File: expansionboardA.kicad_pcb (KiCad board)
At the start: 2 copper layers, 111 x 109.4 mm, 40 parts, among them J1 USB-SERIAL, J3 HDMI_A, P1 USB_C_Plug, U1 MAX3420EECJ, U2 GPIO_U2, U3 AMS1117-3.3, U4 GPIO_U4, U5 MCP3008T-I/SL, U6 TLV320AIC23BIPW, Y1 Crystal

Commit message: Small layout edits
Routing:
- net LED4: track 44.6 -> 42.3 mm
- net LED3: track 47.5 -> 46.6 mm
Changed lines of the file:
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@@
     (property "ki_keywords" "cap capacitor")
     (attr smd)
-    (fp_text reference "C2" (at 0 -1.43 45) (layer "F.SilkS")
+    (fp_text reference "C2" (at -0.833029 -1.885661 45) (layer "F.SilkS")
         (effects (font (size 1 1) (thickness 0.15)))
     )
@@
     (property "ki_keywords" "cap capacitor")
     (attr smd)
-    (fp_text reference "C7" (at 3.1308 0.1256 -270) (layer "F.SilkS")
+    (fp_text reference "C7" (at 2.9972 0.0254 -270) (layer "F.SilkS")
         (effects (font (size 1 1) (thickness 0.15)))
     )
@@
     (property "ki_keywords" "cap capacitor")
     (attr smd)
-    (fp_text reference "C4" (at -3.355917 -0.179605 45) (layer "F.SilkS")
+    (fp_text reference "C4" (at -0.087104 -1.975656 45) (layer "F.SilkS")
         (effects (font (size 1 1) (thickness 0.15)))
     )
@@
     (property "ki_keywords" "quartz ceramic resonator oscillator")
     (attr through_hole)
-    (fp_text reference "Y1" (at -1.75 -3 -225) (layer "B.SilkS")
+    (fp_text reference "Y1" (at -1.752563 -7.848744 -225) (layer "B.SilkS")
         (effects (font (size 1 1) (thickness 0.15)) (justify mirror))
     )
@@
   (via (at 42.926 69.088) (size 0.8) (drill 0.4) (layers "F.Cu" "B.Cu") (net 108))
   (segment (start 33.2232 87.376) (end 31.6992 87.376) (width 0.25) (layer "B.Cu") (net 108))
-  (segment (start 46.99 66.6496) (end 46.99 44.41) (width 0.25) (layer "B.Cu") (net 108))
   (segment (start 45.68 43.18) (end 48.22 43.18) (width 0.25) (layer "B.Cu") (net 108))
   (segment (start 30.9118 84.4296) (end 31.7754 83.566) (width 0.25) (layer "B.Cu") (net 108))
   (segment (start 103.124 44.704) (end 95.25 44.704) (width 0.25) (layer "B.Cu") (net 108))
+  (segment (start 44.704 67.31) (end 46.3296 67.31) (width 0.25) (layer "B.Cu") (net 108))
   (segment (start 103.124 44.704) (end 104.648 43.18) (width 0.25) (layer "B.Cu") (net 108))
   (segment (start 88.646 38.1) (end 79.248 38.1) (width 0.25) (layer "B.Cu") (net 108))
-  (segment (start 42.926 69.088) (end 44.704 67.31) (width 0.25) (layer "B.Cu") (net 108))
   (segment (start 31.7754 83.566) (end 32.512 83.566) (width 0.25) (layer "B.Cu") (net 108))
-  (segment (start 44.704 67.31) (end 46.3296 67.31) (width 0.25) (layer "B.Cu") (net 108))
+  (segment (start 46.3296 67.31) (end 46.9392 66.7004) (width 0.25) (layer "B.Cu") (net 108))
+  (segment (start 42.926 69.088) (end 44.704 67.31) (width 0.25) (layer "B.Cu") (net 108))
   (segment (start 112.268 74.93) (end 105.791 74.93) (width 0.25) (layer "B.Cu") (net 108))
   (segment (start 30.9118 86.5886) (end 30.9118 84.4296) (width 0.25) (layer "B.Cu") (net 108))
   (segment (start 103.124 72.263) (end 103.124 44.704) (width 0.25) (layer "B.Cu") (net 108))
   (segment (start 70.612 29.464) (end 65.106 29.464) (width 0.25) (layer "B.Cu") (net 108))
+  (segment (start 46.9392 66.7004) (end 46.9392 44.4608) (width 0.25) (layer "B.Cu") (net 108))
   (segment (start 33.782 119.6594) (end 33.782 87.9348) (width 0.25) (layer "B.Cu") (net 108))
   (segment (start 106.68 43.18) (end 109.22 43.18) (width 0.25) (layer "B.Cu") (net 108))
-  (segment (start 46.99 44.41) (end 48.22 43.18) (width 0.25) (layer "B.Cu") (net 108))
   (segment (start 82.7786 124.968) (end 39.0906 124.968) (width 0.25) (layer "B.Cu") (net 108))
   (segment (start 39.0906 124.968) (end 33.782 119.6594) (width 0.25) (layer "B.Cu") (net 108))
+  (segment (start 46.9392 44.4608) (end 48.22 43.18) (width 0.25) (layer "B.Cu") (net 108))
   (segment (start 95.25 44.704) (end 88.646 38.1) (width 0.25) (layer "B.Cu") (net 108))
   (segment (start 31.6992 87.376) (end 30.9118 86.5886) (width 0.25) (layer "B.Cu") (net 108))
   (segment (start 104.648 43.18) (end 106.68 43.18) (width 0.25) (layer "B.Cu") (net 108))
-  (segment (start 46.3296 67.31) (end 46.99 66.6496) (width 0.25) (layer "B.Cu") (net 108))
   (segment (start 105.791 74.93) (end 103.124 72.263) (width 0.25) (layer "B.Cu") (net 108))
   (segment (start 82.8294 124.9172) (end 82.7786 124.968) (width 0.25) (layer "B.Cu") (net 108))
@@
   (segment (start 57.125 74.825) (end 49.385 74.825) (width 0.25) (layer "F.Cu") (net 142))
   (segment (start 49.385 74.825) (end 48.22 73.66) (width 0.25) (layer "F.Cu") (net 142))
+  (segment (start 82.036584 32.5738) (end 84.827792 32.5738) (width 0.25) (layer "F.Cu") (net 154))
+  (segment (start 85.277792 32.1238) (end 92.3098 32.1238) (width 0.25) (layer "F.Cu") (net 154))
+  (segment (start 92.3098 32.1238) (end 93.5736 30.86) (width 0.25) (layer "F.Cu") (net 154))
+  (segment (start 84.827792 32.5738) (end 85.277792 32.1238) (width 0.25) (layer "F.Cu") (net 154))
+  (segment (start 80.7174 33.0238) (end 81.586584 33.0238) (width 0.25) (layer "F.Cu") (net 154))
   (segment (start 48.22 66.04) (end 48.22 65.5212) (width 0.25) (layer "F.Cu") (net 154))
-  (segment (start 48.22 65.5212) (end 67.737368 46.003832) (width 0.25) (layer "F.Cu") (net 154))
-  (segment (start 67.737368 46.003832) (end 71.62636 46.003832) (width 0.25) (layer "F.Cu") (net 154))
-  (segment (start 92.3986 32.035) (end 93.5736 30.86) (width 0.25) (layer "F.Cu") (net 154))
-  (segment (start 71.62636 46.003832) (end 85.595192 32.035) (width 0.25) (layer "F.Cu") (net 154))
-  (segment (start 85.595192 32.035) (end 92.3986 32.035) (width 0.25) (layer "F.Cu") (net 154))
-  (segment (start 49.604804 63.5) (end 67.550972 45.553832) (width 0.25) (layer "F.Cu") (net 155))
-  (segment (start 89.4577 31.585) (end 90.1827 30.86) (width 0.25) (layer "F.Cu") (net 155))
-  (segment (start 71.439964 45.553832) (end 85.408796 31.585) (width 0.25) (layer "F.Cu") (net 155))
-  (segment (start 85.408796 31.585) (end 89.4577 31.585) (width 0.25) (layer "F.Cu") (net 155))
+  (segment (start 48.22 65.5212) (end 80.7174 33.0238) (width 0.25) (layer "F.Cu") (net 154))
+  (segment (start 81.586584 33.0238) (end 82.036584 32.5738) (width 0.25) (layer "F.Cu") (net 154))
+  (segment (start 85.091396 31.6738) (end 87.8332 31.6738) (width 0.25) (layer "F.Cu") (net 155))
+  (segment (start 88.647 30.86) (end 90.1827 30.86) (width 0.25) (layer "F.Cu") (net 155))
+  (segment (start 80.531004 32.5738) (end 81.400188 32.5738) (width 0.25) (layer "F.Cu") (net 155))
   (segment (start 48.22 63.5) (end 49.604804 63.5) (width 0.25) (layer "F.Cu") (net 155))
-  (segment (start 67.550972 45.553832) (end 71.439964 45.553832) (width 0.25) (layer "F.Cu") (net 155))
-  (segment (start 85.4974 30.86) (end 86.7918 30.86) (width 0.25) (layer "F.Cu") (net 156))
-  (segment (start 51.508408 60.96) (end 67.364576 45.103832) (width 0.25) (layer "F.Cu") (net 156))
-  (segment (start 71.253568 45.103832) (end 85.4974 30.86) (width 0.25) (layer "F.Cu") (net 156))
-  (segment (start 67.364576 45.103832) (end 71.253568 45.103832) (width 0.25) (layer "F.Cu") (net 156))
+  (segment (start 49.604804 63.5) (end 80.531004 32.5738) (width 0.25) (layer "F.Cu") (net 155))
+  (segment (start 84.641396 32.1238) (end 85.091396 31.6738) (width 0.25) (layer "F.Cu") (net 155))
+  (segment (start 81.400188 32.5738) (end 81.850188 32.1238) (width 0.25) (layer "F.Cu") (net 155))
+  (segment (start 81.850188 32.1238) (end 84.641396 32.1238) (width 0.25) (layer "F.Cu") (net 155))
+  (segment (start 87.8332 31.6738) (end 88.647 30.86) (width 0.25) (layer "F.Cu") (net 155))
+  (segment (start 51.508408 60.96) (end 80.344608 32.1238) (width 0.25) (layer "F.Cu") (net 156))
+  (segment (start 85.2688 30.86) (end 86.7918 30.86) (width 0.25) (layer "F.Cu") (net 156))
   (segment (start 48.22 60.96) (end 51.508408 60.96) (width 0.25) (layer "F.Cu") (net 156))
-  (segment (start 71.067172 44.653832) (end 83.4009 32.320104) (width 0.25) (layer "F.Cu") (net 157))
-  (segment (start 67.17818 44.653832) (end 71.067172 44.653832) (width 0.25) (layer "F.Cu") (net 157))
-  (segment (start 83.4009 32.320104) (end 83.4009 30.86) (width 0.25) (layer "F.Cu") (net 157))
+  (segment (start 84.455 31.6738) (end 85.2688 30.86) (width 0.25) (layer "F.Cu") (net 156))
+  (segment (start 80.344608 32.1238) (end 81.213792 32.1238) (width 0.25) (layer "F.Cu") (net 156))
+  (segment (start 81.663792 31.6738) (end 84.455 31.6738) (width 0.25) (layer "F.Cu") (net 156))
+  (segment (start 81.213792 32.1238) (end 81.663792 31.6738) (width 0.25) (layer "F.Cu") (net 156))
   (segment (start 48.22 58.42) (end 53.412012 58.42) (width 0.25) (layer "F.Cu") (net 157))
-  (segment (start 53.412012 58.42) (end 67.17818 44.653832) (width 0.25) (layer "F.Cu") (net 157))
-  (segment (start 70.880776 44.203832) (end 80.01 35.074608) (width 0.25) (layer "F.Cu") (net 158))
-  (segment (start 80.01 35.074608) (end 80.01 30.86) (width 0.25) (layer "F.Cu") (net 158))
+  (segment (start 80.158212 31.6738) (end 81.027396 31.6738) (width 0.25) (layer "F.Cu") (net 157))
+  (segment (start 81.027396 31.6738) (end 81.841196 30.86) (width 0.25) (layer "F.Cu") (net 157))
+  (segment (start 81.841196 30.86) (end 83.4009 30.86) (width 0.25) (layer "F.Cu") (net 157))
+  (segment (start 53.412012 58.42) (end 80.158212 31.6738) (width 0.25) (layer "F.Cu") (net 157))
+  (segment (start 80.01 31.185616) (end 80.01 30.86) (width 0.25) (layer "F.Cu") (net 158))
+  (segment (start 55.315616 55.88) (end 80.01 31.185616) (width 0.25) (layer "F.Cu") (net 158))
   (segment (start 48.22 55.88) (end 55.315616 55.88) (width 0.25) (layer "F.Cu") (net 158))
-  (segment (start 66.991784 44.203832) (end 70.880776 44.203832) (width 0.25) (layer "F.Cu") (net 158))
-  (segment (start 55.315616 55.88) (end 66.991784 44.203832) (width 0.25) (layer "F.Cu") (net 158))
   (segment (start 89.696427 94.453573) (end 89.488571 94.453573) (width 0.25) (layer "F.Cu") (net 159))
   (segment (start 89.488571 94.453573) (end 84.9122 89.877202) (width 0.25) (layer "F.Cu") (net 159))

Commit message: Board updated
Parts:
- moved ADC1 10.0 mm to (35.1, 93.6)
- moved C2 1.83 mm to (82.9, 102.7), turned to 0 degrees
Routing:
- net USBSCLK: track 49.7 -> 68.5 mm
- net HPOUTRIGHT: track 74.0 -> 91.4 mm
- net USBMISO: track 53.8 -> 68.5 mm
- net LINEOUTRIGHT: track 78.7 -> 91.6 mm
- net USBGPX: track 57.4 -> 68.5 mm
- net ADCH1: track 24.0 -> 34.9 mm
- net USBMOSI: track 58.6 -> 68.5 mm
- net ADCH3: track 19.7 -> 29.2 mm
- net ADCH4: track 15.5 -> 24.8 mm
- net ADCH5: track 16.3 -> 25.4 mm
- net ADCH2: track 22.1 -> 31.2 mm
- net ADCH6: track 9.13 -> 18.2 mm
- net ADCH0: track 28.9 -> 37.9 mm
- net ADCH7: track 12.4 -> 21.1 mm
- net LINEOUTLEFT: track 83.3 -> 91.7 mm
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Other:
- board text added: "DVI OUT"
- board text added: "INT"
- board text added: "REG 3V"
- board text removed: "Video Out"

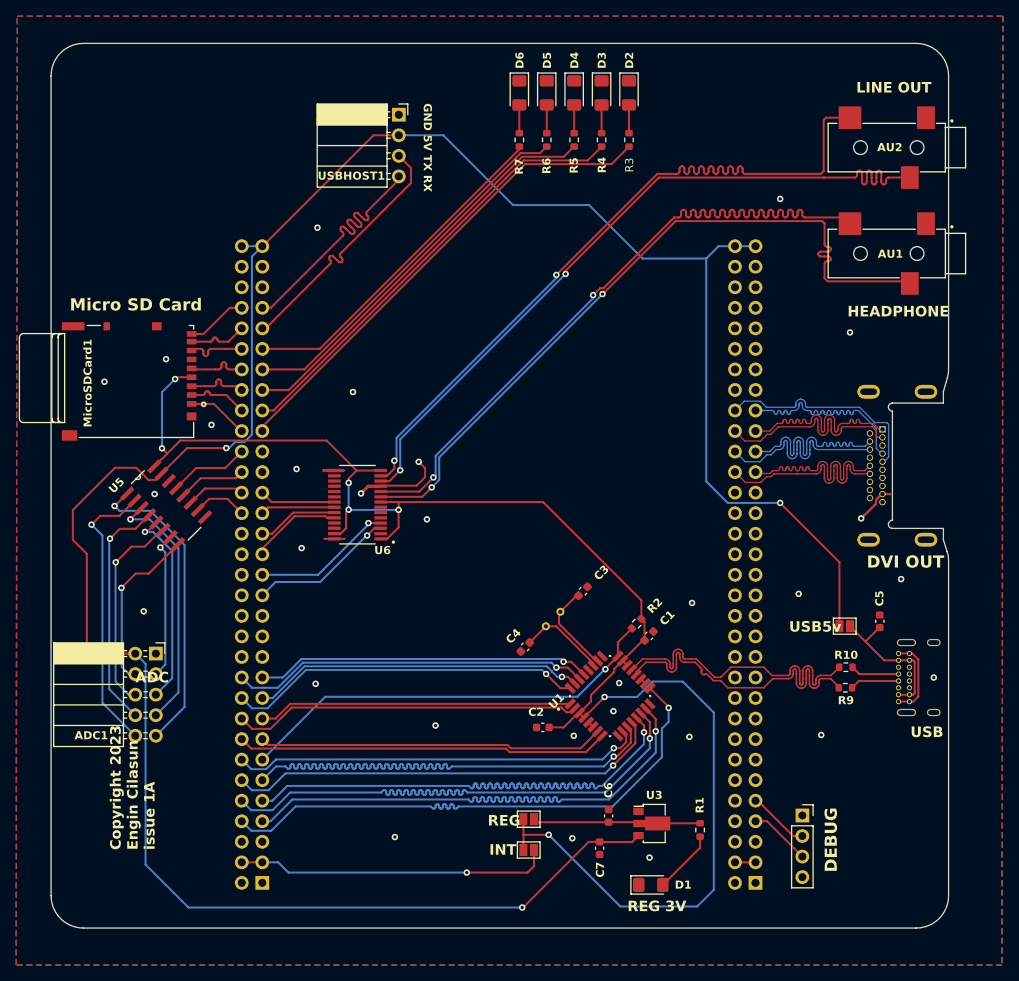
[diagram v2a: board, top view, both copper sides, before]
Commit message: Updated schematic with correct parts Built gerber files
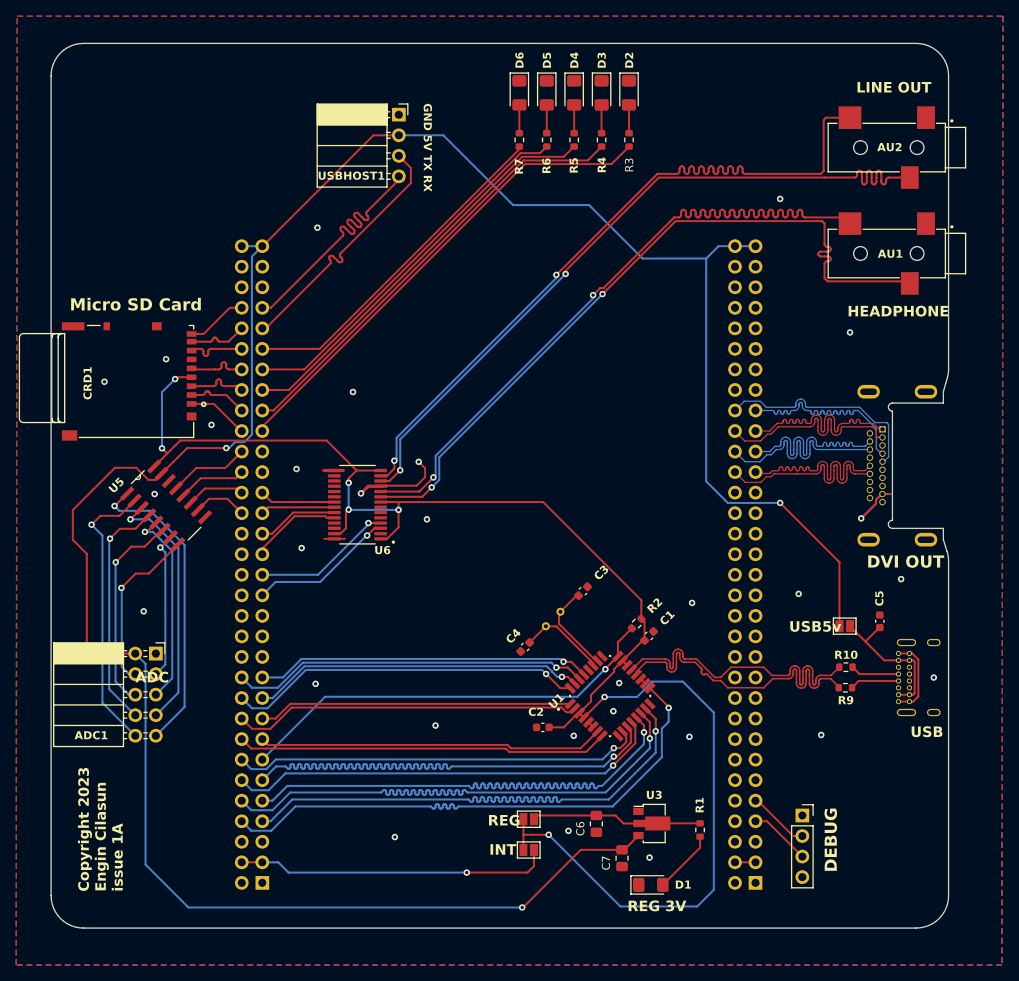
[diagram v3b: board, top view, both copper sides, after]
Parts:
- C6, C7: footprint Capacitor_SMD:C_0603_1608Metric -> Capacitor_SMD:C_0805_2012Metric_Pad1.18x1.45mm_HandSolder
- J1: value USB-SERIAL -> DEBUG
- moved C7 3.04 mm to (92.7, 118.9)
- moved C6 1.82 mm to (89.5, 114.6), turned to -90 degrees
- renumbered MicroSDCard1 to CRD1
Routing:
- net 5V: track 301.7 -> 300.6 mm

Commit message: Updated board with USB A host connector
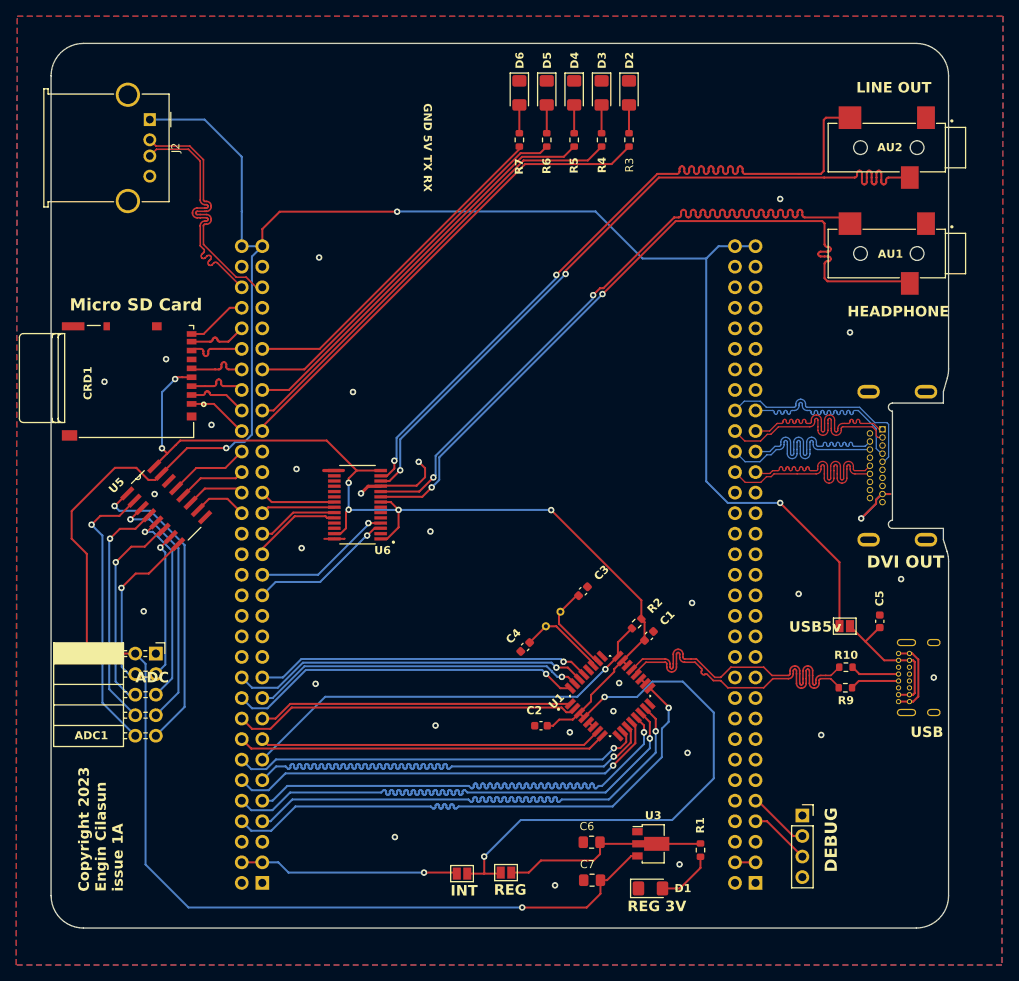
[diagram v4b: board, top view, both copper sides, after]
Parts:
- removed USBHOST1: Conn_01x4_Socket, Connector_PinSocket_2.54mm:PinSocket_1x04_P2.54mm_Horizontal
- added J2: USB_A_Stacked, Connector_USB:USB_A_Molex_67643_Horizontal, F.Cu at (34.3, 27.5)
- moved JP6 8.75 mm to (72.9, 120.8), turned to 180 degrees
- moved JP5 7.18 mm to (78.4, 120.7)
- moved C7 4.59 mm to (89.0, 121.6), turned to 180 degrees
- moved U3 2.52 mm to (96.6, 117.1)
- moved R1 2.49 mm to (102.4, 117.9)
- moved C6 2.34 mm to (89.0, 116.9), turned to 180 degrees
- moved D1 0.43 mm to (96.2, 122.6)
- moved C2 0.31 mm to (82.7, 102.5)
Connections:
- U2 pad 55: USBTX -> unconnected-(U2-Pin_55-Pad55)
- U2 pad 57: USBRX -> unconnected-(U2-Pin_57-Pad57)
- U2 pad 59: unconnected-(U2-Pin_59-Pad59) -> USBD1_N
- U2 pad 60: unconnected-(U2-Pin_60-Pad60) -> USBD1_P
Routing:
- net USBTX: track 32.0 -> 0.00 mm
- net USBD1_N: track 0.00 -> 31.9 mm
- net USBRX: track 31.9 -> 0.00 mm
- net USBD1_P: track 0.00 -> 31.8 mm
- net 5V: track 300.6 -> 318.3 mm, vias 3 -> 4
- net 3V3: track 39.0 -> 27.2 mm
- net /input3v3: track 198.9 -> 191.1 mm, vias 7 -> 8
- net REG3V3: track 21.2 -> 25.9 mm
- net Net-(D1-A): track 7.88 -> 7.12 mm

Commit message: Updated board
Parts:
- C1, C2, C3, C4, C5: footprint Capacitor_SMD:C_0603_1608Metric -> Capacitor_SMD:C_0603_1608Metric_Pad1.08x0.95mm_HandSolder
- R1, R10, R2, R3, R4, R5, R6, R7, R9: footprint Resistor_SMD:R_0603_1608Metric -> Resistor_SMD:R_0603_1608Metric_Pad0.98x0.95mm_HandSolder
- U3: footprint Package_TO_SOT_SMD:SOT-89-3 -> Package_TO_SOT_SMD:SOT-89-3_Handsoldering
- moved D3 28.1 mm to (62.1, 23.9)
- moved D4 28.1 mm to (58.7, 23.9)
- moved D5 28.1 mm to (55.3, 23.9)
- moved D6 28.1 mm to (51.9, 23.9)
- moved R7 28.1 mm to (51.9, 29.8)
- moved R3 28.1 mm to (65.5, 29.8)
- moved R4 28.1 mm to (62.1, 29.8)
- moved R5 28.1 mm to (58.7, 29.8)
- moved R6 28.1 mm to (55.3, 29.8)
- moved D2 28.1 mm to (65.5, 23.9)
- moved C3 0.21 mm to (87.9, 85.6)
- moved C2 0.19 mm to (82.5, 102.5)
- moved C4 0.13 mm to (80.6, 92.8)
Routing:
- net LED3: track 46.6 -> 31.5 mm
- net LED2: track 51.0 -> 36.8 mm
- net LED1: track 55.5 -> 41.9 mm
- net LED4: track 42.3 -> 29.6 mm
- net LED0: track 60.2 -> 48.0 mm
- net 5V: track 318.3 -> 318.9 mm
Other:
- board text added: "5V D- D+ GND"
- board text added: "Copyright 2023 Engin Cilasun issue 1B"
- board text added: "DEBUG UART"
- board text added: "REG 3v3"
- board text added: "USB Host"
- board text added: "USB-C Power"
- board text removed: "Copyright 2023 Engin Cilasun issue 1A"
- board text removed: "DEBUG"
- board text removed: "GND 5V TX RX"
- board text removed: "REG 3V"
- board text removed: "USB"
